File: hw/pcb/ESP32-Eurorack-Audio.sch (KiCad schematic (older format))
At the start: 10 parts

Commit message: wm8978 PCB design files
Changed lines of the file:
@@
 encoding utf-8
 Sheet 1 6
-Title "CTAG TBD Eurorack Audio Module"
-Date "2020-03-18"
-Rev "B"
+Title "CTAG-TBD"
+Date "2020-06-06"
+Rev "C"
 Comp "(c) Robert Manzke 2020"
 Comment1 "https://creativecommons.org/licenses/by-nc-sa/4.0/"
@@
 	3350 2850 3800 2850
 Wire Wire Line
-	3800 2950 3350 2950
+	3800 2950 3650 2950
 Wire Wire Line
 	3350 3050 3800 3050
@@
 $EndSheet
 $Sheet
-S 6050 2700 550  850
+S 6050 2600 550  950
 U 5B69D59C
 F0 "CODEC" 50
@@
 F7 "LRCLK" I L 6050 3250 50
 F8 "ADCDAT" O L 6050 3450 50
+F9 "MCLK" I L 6050 2700 50
 $EndSheet
 $Sheet
@@
 Wire Wire Line
 	6050 4650 5800 4650
+Wire Wire Line
+	6050 2700 5950 2700
+Wire Wire Line
+	5950 2700 5950 2350
+Wire Wire Line
+	5950 2350 3650 2350
+Wire Wire Line
+	3650 2350 3650 2950
+Connection ~ 3650 2950
+Wire Wire Line
+	3650 2950 3350 2950
 $EndSCHEMATC

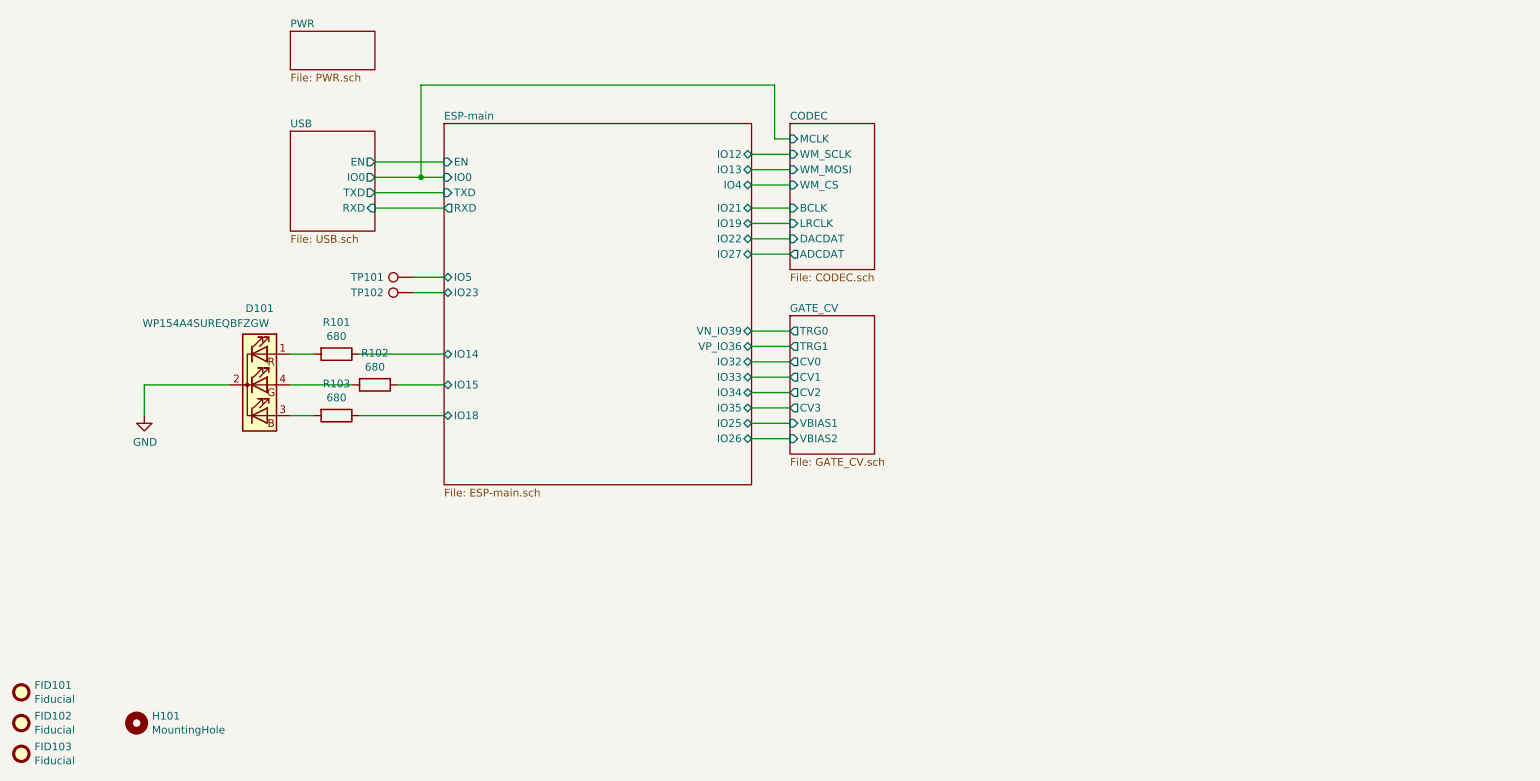
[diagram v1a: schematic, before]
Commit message: fixed severe PCB issue, clearance of ground fills was too small, could lead to thermal instability
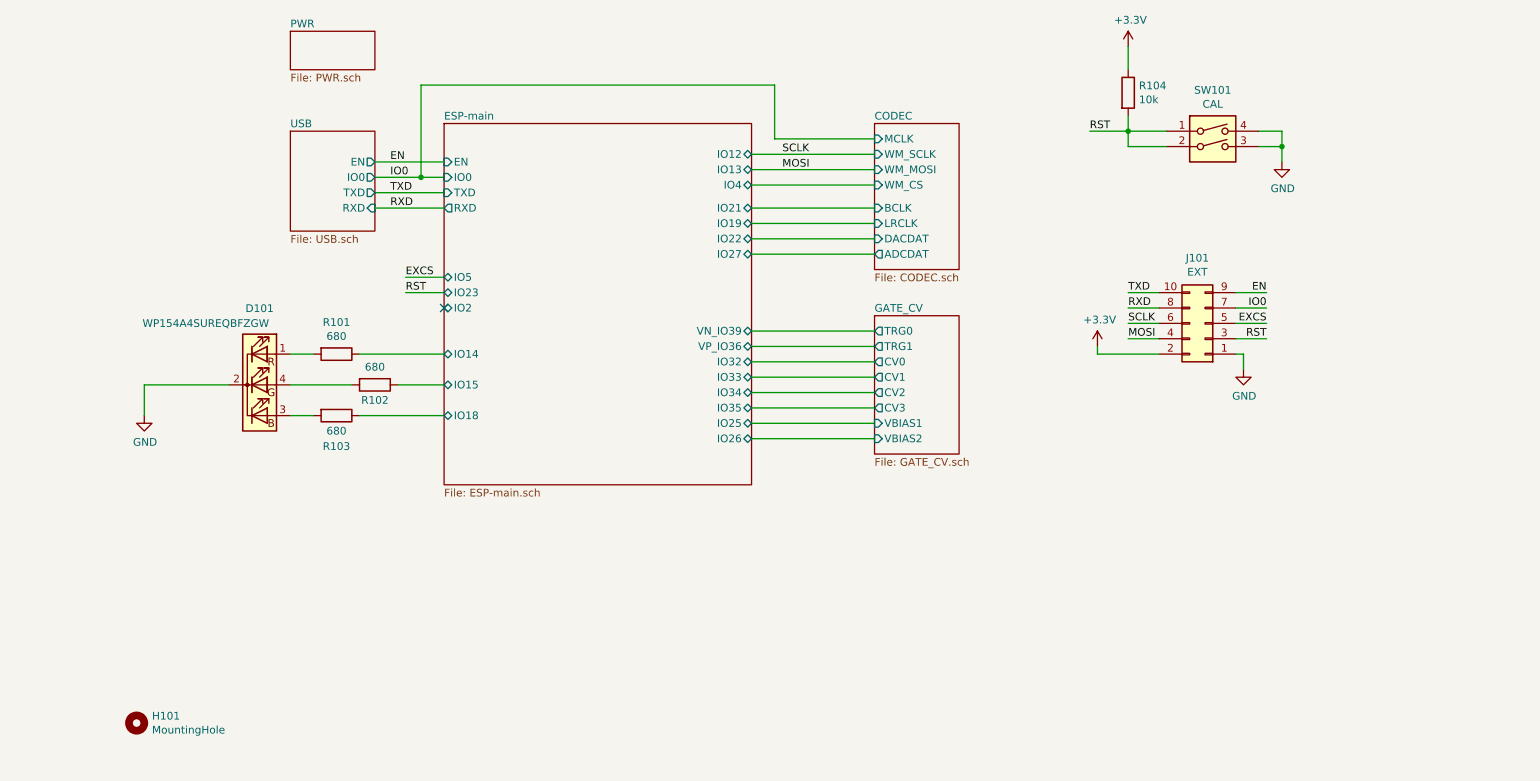
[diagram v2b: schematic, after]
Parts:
- removed FID101, FID102, FID103: Fiducial, Fiducial:Fiducial_1mm_Mask2mm, symbol Mechanical:Fiducial
- removed TP101, TP102: ~, TestPoint:TestPoint_Keystone_5019_Minature, symbol Connector:TestPoint
- added J101: EXT, Connector_PinHeader_2.54mm:PinHeader_2x05_P2.54mm_Vertical_SMD, symbol Connector_Generic:Conn_02x05_Odd_Even
- added R104: 10k, Resistor_SMD:R_0402_1005Metric, symbol Device:R
- added SW101: CAL, switches:PTS810, symbol Switch:SW_DIP_x02
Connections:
- net GND: now also J101.1 (Pin_1), SW101.3, SW101.4
- new net +3V3: J101.2 (Pin_2), R104.1
- new net EN: J101.9 (Pin_9)
- new net EXCS: J101.5 (Pin_5)
- new net IO0: J101.7 (Pin_7)
- new net MOSI: J101.4 (Pin_4)
- new net RST: J101.3 (Pin_3), R104.2, SW101.1, SW101.2
- new net RXD: J101.8 (Pin_8)
- new net SCLK: J101.6 (Pin_6)
- new net TXD: J101.10 (Pin_10)
- no-connect marks 0 -> 1

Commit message: Updated Eurorack hw to Rev. H
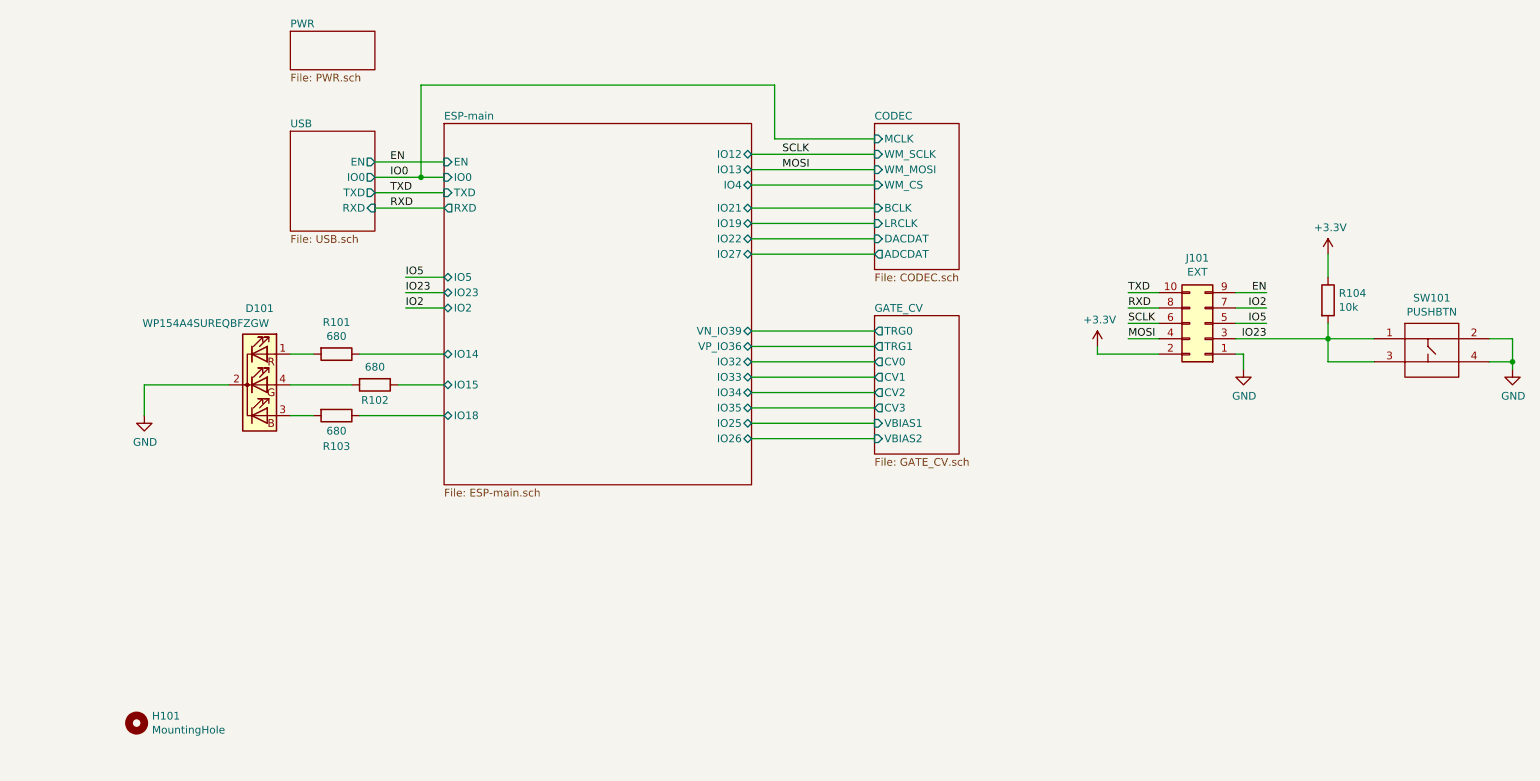
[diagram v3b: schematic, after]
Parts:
- removed SW101: CAL, switches:PTS810, symbol Switch:SW_DIP_x02
- added SW101: PUSHBTN, switches:TactilePB_6x6, symbol special-ics:PUSHBTN
- D101: footprint LED_THT:LED_D5.0mm-4_RGB -> LED_THT:LED_D5.0mm-4_RGB_Staggered_Pins
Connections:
- net GND: now also SW101.2, SW101.4
- net IO0: no longer J101.7 (Pin_7)
- net EXCS renamed IO5
- net RST renamed IO23
- net IO23: now also SW101.1, SW101.3
- new net IO2: J101.7 (Pin_7)
- no-connect marks 1 -> 0
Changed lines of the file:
@@
 Sheet 1 6
 Title "ESP32 Eurorack Audio Module"
-Date "2020-08-18"
-Rev "G"
-Comp "(c) Robert Manzke 2020"
+Date "2021-10-05"
+Rev "H"
+Comp "(c) Robert Manzke 2021"
 Comment1 "https://creativecommons.org/licenses/by-nc-sa/4.0/"
 Comment2 "Licensed under CC BY-NC-SA 4.0"
@@
 F 0 "D101" H 2600 4797 50  0000 C CNN
 F 1 "WP154A4SUREQBFZGW" H 2250 4700 50  0000 C CNN
-F 2 "LED_THT:LED_D5.0mm-4_RGB" H 2600 4250 50  0001 C CNN
+F 2 "LED_THT:LED_D5.0mm-4_RGB_Staggered_Pins" H 2600 4250 50  0001 C CNN
 F 3 "~" H 2600 4250 50  0001 C CNN
 	1    2600 4300
@@
 	3650 2950 3350 2950
 Text Label 3550 3700 0    50   ~ 0
-RST
-Wire Wire Line
-	8500 2750 8250 2750
-Wire Wire Line
-	8250 2750 8250 2650
-Wire Wire Line
-	8250 2650 8500 2650
-Wire Wire Line
-	8250 2650 8000 2650
-Connection ~ 8250 2650
-Text Label 8000 2650 0    50   ~ 0
-RST
-$Comp
-L Device:R R104
-U 1 1 5E9015EA
-P 8250 2400
-F 0 "R104" H 8320 2446 50  0000 L CNN
-F 1 "10k" H 8320 2355 50  0000 L CNN
-F 2 "Resistor_SMD:R_0402_1005Metric" V 8180 2400 50  0001 C CNN
-F 3 "~" H 8250 2400 50  0001 C CNN
-	1    8250 2400
-	1    0    0    -1
-$EndComp
-Wire Wire Line
-	8250 2550 8250 2650
-$Comp
-L power:+3.3V #PWR0103
-U 1 1 5E90752D
-P 8250 2100
-F 0 "#PWR0103" H 8250 1950 50  0001 C CNN
-F 1 "+3.3V" H 8265 2273 50  0000 C CNN
-F 2 "" H 8250 2100 50  0001 C CNN
-F 3 "" H 8250 2100 50  0001 C CNN
-	1    8250 2100
-	1    0    0    -1
-$EndComp
-Wire Wire Line
-	8250 2100 8250 2250
-$Comp
-L power:GND #PWR0105
-U 1 1 5E9097E9
-P 9250 2850
-F 0 "#PWR0105" H 9250 2600 50  0001 C CNN
-F 1 "GND" H 9255 2677 50  0000 C CNN
-F 2 "" H 9250 2850 50  0001 C CNN
-F 3 "" H 9250 2850 50  0001 C CNN
-	1    9250 2850
-	1    0    0    -1
-$EndComp
-Wire Wire Line
-	9100 2650 9250 2650
-Wire Wire Line
-	9250 2650 9250 2750
-Wire Wire Line
-	9100 2750 9250 2750
-Connection ~ 9250 2750
+IO23
 Text Label 6000 2800 0    50   ~ 0
 SCLK
@@
 Wire Wire Line
 	5800 2900 6600 2900
-$Comp
-L Switch:SW_DIP_x02 SW101
-U 1 1 5E8F9FEC
-P 8800 2750
-F 0 "SW101" H 8800 3117 50  0000 C CNN
-F 1 "CAL" H 8800 3026 50  0000 C CNN
-F 2 "switches:PTS810" H 8800 2750 50  0001 C CNN
-F 3 "~" H 8800 2750 50  0001 C CNN
-	1    8800 2750
-	1    0    0    -1
-$EndComp
-Wire Wire Line
-	9250 2750 9250 2850
-NoConn ~ 3800 3800
-Text Label 3550 3600 0    50   ~ 0
-EXCS
 $Comp
 L power:GND #PWR0106
@@
 Wire Wire Line
 	8950 3900 9150 3900
-Wire Wire Line
-	8950 4000 9150 4000
 Text Label 9150 4000 2    50   ~ 0
-RST
+IO23
 Text Label 8250 3900 0    50   ~ 0
 SCLK
@@
 MOSI
 Text Label 9150 3900 2    50   ~ 0
-EXCS
+IO5
 $Comp
 L Connector_Generic:Conn_02x05_Odd_Even J101
@@
 Text Label 8250 3700 0    50   ~ 0
 TXD
-Text Label 9150 3800 2    50   ~ 0
-IO0
 Text Label 9150 3700 2    50   ~ 0
 EN
+Wire Wire Line
+	3800 3800 3550 3800
+Text Label 3550 3800 0    50   ~ 0
+IO2
+Text Label 9150 3800 2    50   ~ 0
+IO2
+Text Label 3550 3600 0    50   ~ 0
+IO5
+$Comp
+L Device:R R104
+U 1 1 615C8DFC
+P 9550 3750
+F 0 "R104" H 9620 3796 50  0000 L CNN
+F 1 "10k" H 9620 3705 50  0000 L CNN
+F 2 "Resistor_SMD:R_0402_1005Metric" V 9480 3750 50  0001 C CNN
+F 3 "~" H 9550 3750 50  0001 C CNN
+	1    9550 3750
+	1    0    0    -1
+$EndComp
+Wire Wire Line
+	9550 4000 9550 3900
+Wire Wire Line
+	8950 4000 9550 4000
+$Comp
+L power:+3.3V #PWR0105
+U 1 1 615CA249
+P 9550 3450
+F 0 "#PWR0105" H 9550 3300 50  0001 C CNN
+F 1 "+3.3V" H 9565 3623 50  0000 C CNN
+F 2 "" H 9550 3450 50  0001 C CNN
+F 3 "" H 9550 3450 50  0001 C CNN
+	1    9550 3450
+	1    0    0    -1
+$EndComp
+Wire Wire Line
+	9550 3450 9550 3600
+$Comp
+L special-ics:PUSHBTN SW101
+U 1 1 615EBE07
+P 10050 3850
+F 0 "SW101" H 10225 3965 50  0000 C CNN
+F 1 "PUSHBTN" H 10225 3874 50  0000 C CNN
+F 2 "switches:TactilePB_6x6" H 10050 3850 50  0001 C CNN
+F 3 "" H 10050 3850 50  0001 C CNN
+	1    10050 3850
+	1    0    0    -1
+$EndComp
+Wire Wire Line
+	9550 4000 9850 4000
+Connection ~ 9550 4000
+Wire Wire Line
+	9550 4000 9550 4150
+Wire Wire Line
+	9550 4150 9850 4150
+$Comp
+L power:GND #PWR0107
+U 1 1 615EE4ED
+P 10750 4200
+F 0 "#PWR0107" H 10750 3950 50  0001 C CNN
+F 1 "GND" H 10755 4027 50  0000 C CNN
+F 2 "" H 10750 4200 50  0001 C CNN
+F 3 "" H 10750 4200 50  0001 C CNN
+	1    10750 4200
+	1    0    0    -1
+$EndComp
+Wire Wire Line
+	10600 4150 10750 4150
+Wire Wire Line
+	10750 4150 10750 4200
+Wire Wire Line
+	10600 4000 10750 4000
+Wire Wire Line
+	10750 4000 10750 4150
+Connection ~ 10750 4150
 $EndSCHEMATC
